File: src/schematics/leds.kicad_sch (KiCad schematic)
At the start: 6 parts

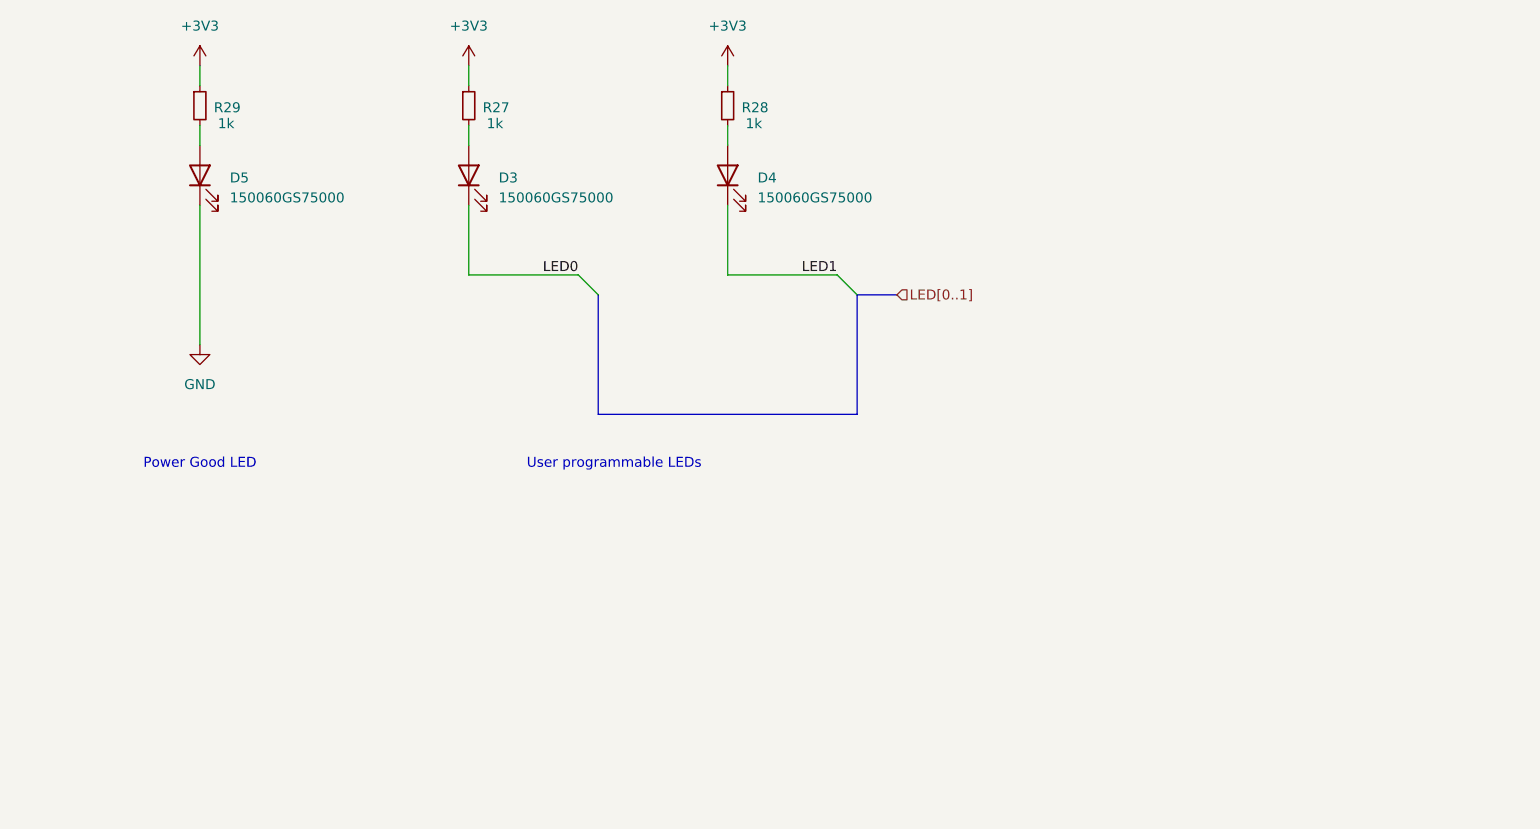
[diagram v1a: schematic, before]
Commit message: Add notes on the schematic
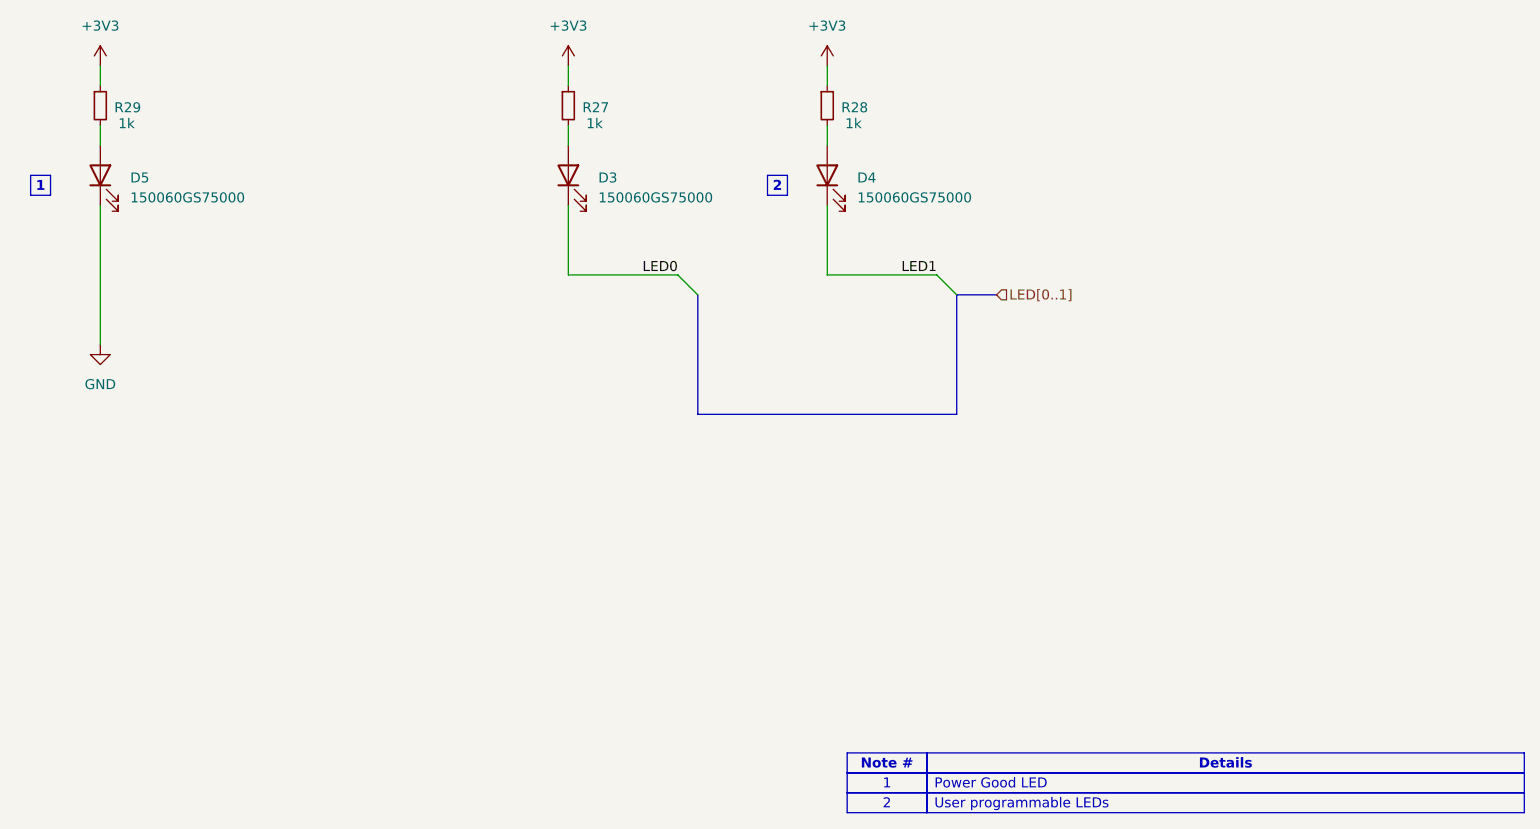
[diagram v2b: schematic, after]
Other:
- note removed: "Power Good LED"
- note removed: "User programmable LEDs"
- moved on the sheet: D3, D4, D5, R27, R28, R29

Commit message: Route the board power supply (#89)
* Replaces the inductors for smaller ones

* Starts routing the power supply

* Starts routing power

* Start adding power planes

* Adds decoupling capacitors

* Adds routing of the power sequencing

* Add routing for SRAM

* Route the SRAM data pins

* Finish routing the SRAM

* Route the SDRAM

* Move 1.8v converter to other side of the board

* Start routing DDR2 data lanes

* Use 0402 resistors instead of 0201 for emmc termination

* Route signals from DDR2 to FPGA bank

* Update routing of emmc

* Route the DDR2 without length matching

* Add length matching for DDR on L4 and L6. Todo L1 and redo L6

* Update routing of DDR2 L6 traces. Todo L1

* Finish routing of ddr2 traces

* Update power layer to support stripline for ddr2

* Fixed mechanical holes
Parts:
- R27, R28, R29: footprint Resistor_SMD:R_0603_1608Metric -> Resistor_SMD:R_0402_1005Metric
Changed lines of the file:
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@@
 			)
 		)
-		(property "Footprint" "Resistor_SMD:R_0603_1608Metric"
+		(property "Footprint" "Resistor_SMD:R_0402_1005Metric"
 			(at 190.5 80.01 0)
 			(effects
@@
 			)
 		)
-		(property "Footprint" "Resistor_SMD:R_0603_1608Metric"
+		(property "Footprint" "Resistor_SMD:R_0402_1005Metric"
 			(at 157.48 80.01 0)
 			(effects
@@
 			)
 		)
-		(property "Footprint" "Resistor_SMD:R_0603_1608Metric"
+		(property "Footprint" "Resistor_SMD:R_0402_1005Metric"
 			(at 97.79 80.01 0)
 			(effects

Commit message: Add bom components
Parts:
- D3, D4, D5: value 150060GS75000 -> Green; MPN (none) -> 150060GS75000; Manufacturer (none) -> Wurth Elektronik; Mouting Technology (none) -> SMD
- R27, R28, R29: MPN (none) -> CRCW04021K00FKEE; Manufacturer (none) -> Vishay; Mouting Technology (none) -> SMD
